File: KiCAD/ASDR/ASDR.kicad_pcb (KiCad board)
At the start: 2 copper layers, 50 x 100 mm, 43 parts, among them J1 IN, J2 OUT, J3 OUT, J4 Conn_01x03, J5 Conn_01x03, Q1 BC550, Q2 BC550, Q3 BC550, Q4 BC547, SW1 SW_SPDT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

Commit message: Review
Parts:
- R7, R8: value 100 -> 100R
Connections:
- J1 pad G: Net-(J1-PadG) -> GND
- J1 pad S: Net-(J1-PadG) -> GND
- RV2 pad 1: Net-(D2-K) -> Net-(R10-Pad1)
- RV2 pad 3: Net-(R10-Pad1) -> Net-(D2-K)
- RV3 pad 1: Net-(R7-Pad1) -> Net-(D3-A)
- RV3 pad 3: Net-(D3-A) -> Net-(R7-Pad1)
- RV4 pad 1: Net-(R8-Pad1) -> Net-(D4-K)
- RV4 pad 3: Net-(D4-K) -> Net-(R8-Pad1)
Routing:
- net Net-(Q1-C): track 3.88 -> 18.0 mm
- net Net-(U3B--): track 2.54 -> 10.8 mm
- net Net-(D4-K): track 13.8 -> 7.82 mm
- net Net-(D3-A): track 7.82 -> 12.8 mm
- net Net-(R10-Pad1): track 8.52 -> 12.8 mm
- net Net-(D2-K): track 21.4 -> 23.9 mm
- net Net-(R7-Pad1): track 16.8 -> 14.3 mm
- net Net-(R8-Pad1): track 15.3 -> 16.8 mm
- net Net-(Q2-C): track 51.4 -> 50.4 mm

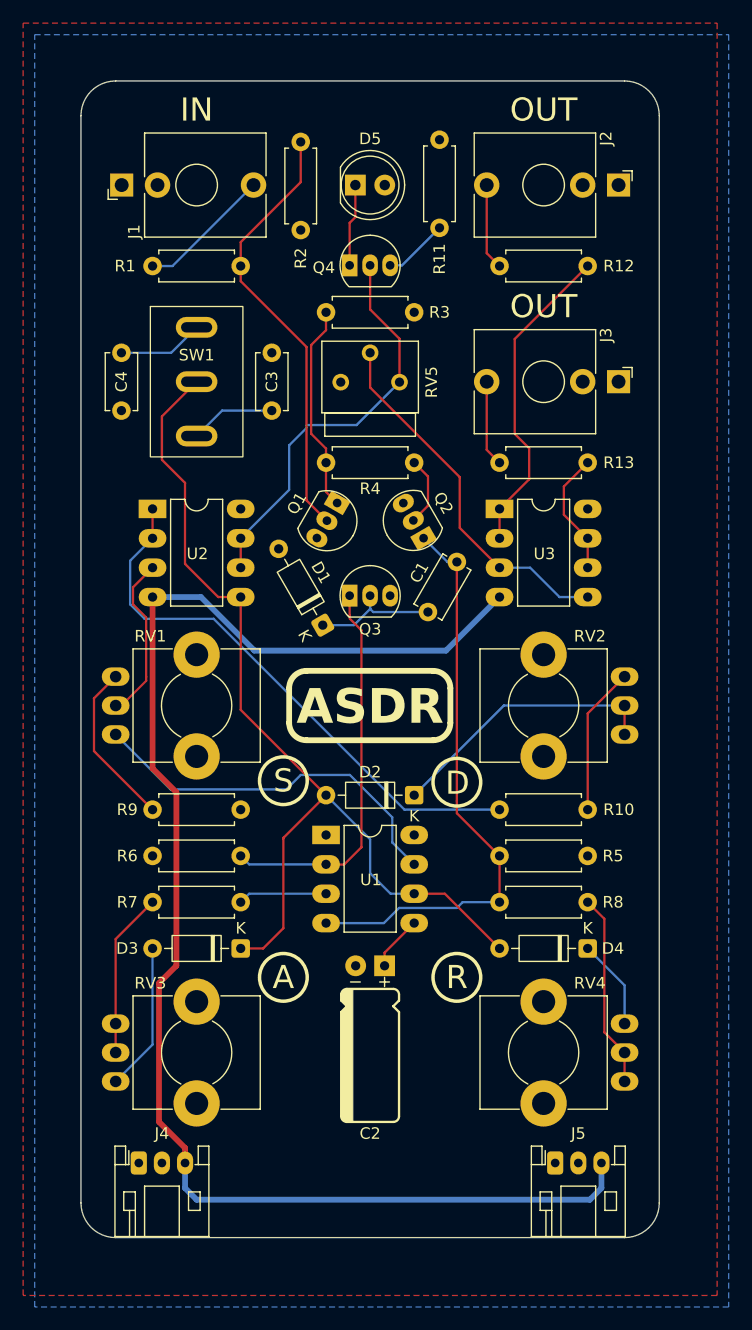
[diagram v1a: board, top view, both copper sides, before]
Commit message: ADSR Rearrange
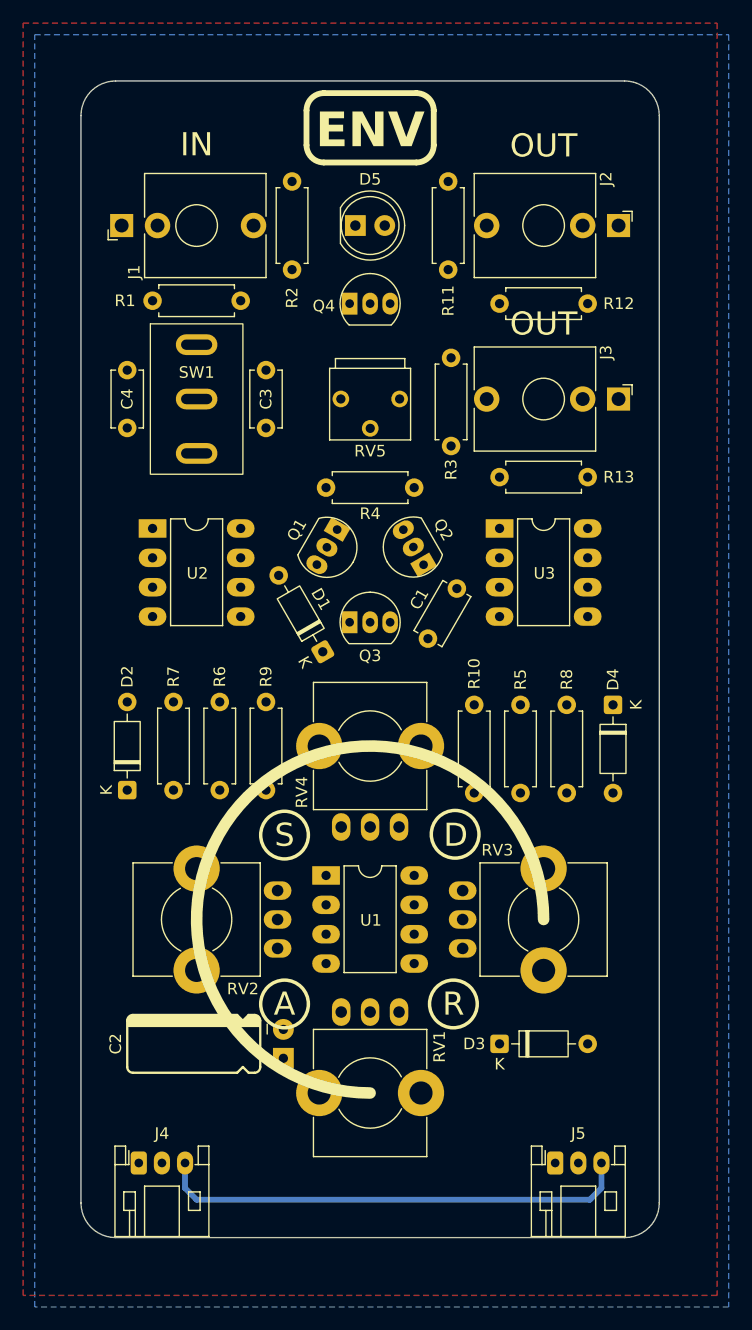
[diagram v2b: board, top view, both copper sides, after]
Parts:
- moved Ref** 48.1 mm to (136.0, 57.0)
- moved Ref** 48.0 mm to (164.2, 56.8)
- moved RV1 36.7 mm to (150.0, 137.5), turned to 180 degrees
- moved RV2 35.2 mm to (135.0, 122.5)
- moved RV3 32.1 mm to (165.0, 122.5)
- moved RV4 30.5 mm to (150.0, 107.5), turned to 0 degrees
- moved D2 24.8 mm to (129.0, 111.3), turned to 90 degrees
- moved D3 23.9 mm to (161.2, 133.2), turned to 0 degrees
- moved D4 21.2 mm to (171.0, 103.9), turned to -90 degrees
- moved R7 17.4 mm to (133.0, 103.7), turned to -90 degrees
- moved R8 17.2 mm to (167.0, 103.9), turned to -90 degrees
- moved R3 15.8 mm to (157.0, 81.6), turned to 90 degrees
- moved R6 13.4 mm to (137.0, 103.7), turned to -90 degrees
- moved R10 13.4 mm to (159.0, 103.9), turned to -90 degrees
- moved C2 10.1 mm to (142.5, 133.3), turned to 90 degrees
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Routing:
- net VSS: track 126.4 -> 41.2 mm
- net Net-(D2-A): track 83.7 -> 0.00 mm
- net Net-(Q2-C): track 50.4 -> 0.00 mm
- net Net-(U2A--): track 48.3 -> 0.00 mm
- net Net-(Q1-B): track 38.0 -> 0.00 mm
- net Net-(Q4-B): track 35.4 -> 0.00 mm
- net Net-(Q3-C): track 33.5 -> 0.00 mm
- net Net-(U1-DIS): track 32.8 -> 0.00 mm
- net Net-(U3A-+): track 31.9 -> 0.00 mm
- net Net-(U3A--): track 27.7 -> 0.00 mm
- net Net-(D2-K): track 23.9 -> 0.00 mm
- net Net-(Q1-C): track 18.0 -> 0.00 mm
- net Net-(R8-Pad1): track 16.8 -> 0.00 mm
- net Net-(R9-Pad2): track 15.4 -> 0.00 mm
- net Net-(U2A-+): track 14.5 -> 0.00 mm
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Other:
- board text added: "ENV"
- board text removed: "ASDR"

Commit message: VCF PCB
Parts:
- moved R13 0.95 mm to (161.2, 85.2)
- moved R3 0.38 mm to (156.7, 81.4)
- moved R11 0.15 mm to (156.6, 58.7)
- moved R2 0.15 mm to (143.4, 66.3)
- turned RV5 to 0 degrees
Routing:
- net Net-(D2-A): track 0.00 -> 110.3 mm, vias 0 -> 1
- net VSS: track 41.2 -> 122.2 mm
- net Net-(Q2-C): track 0.00 -> 52.0 mm, vias 0 -> 1
- net Net-(U2A-+): track 0.00 -> 49.8 mm
- net Net-(U2A--): track 0.00 -> 42.1 mm, vias 0 -> 1
- net Net-(R7-Pad1): track 0.00 -> 38.8 mm, vias 0 -> 1
- net Net-(Q3-C): track 0.00 -> 37.8 mm
- net Net-(Q1-B): track 0.00 -> 36.6 mm
- net Net-(Q4-B): track 0.00 -> 33.0 mm
- net Net-(U3A-+): track 0.00 -> 32.1 mm
- net Net-(R9-Pad2): track 0.00 -> 31.6 mm
- net Net-(R10-Pad1): track 0.00 -> 27.5 mm, vias 0 -> 1
- net Net-(U3A--): track 0.00 -> 25.2 mm
- net Net-(R8-Pad1): track 0.00 -> 24.6 mm
- net Net-(D2-K): track 0.00 -> 23.9 mm
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
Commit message: VCF PCB
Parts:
- C2: footprint HackSynth:CP_Radial_D5.2mm_P2.50mm_LayDown -> HackSynth:CP_Radial_D4.0mm_P1.50mm
- moved C2 22.9 mm to (165.0, 137.5), turned to 0 degrees
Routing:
- net Net-(U1-CV): track 17.1 -> 34.9 mm

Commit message: Footprint Edits
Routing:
- net Net-(U1-CV): track 34.9 -> 17.8 mm
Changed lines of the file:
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@@
 		)
 		(group ""
-			(members "01d04b5b-5a68-4add-86a7-c921b8d4927d" "22b10ea6-8a0e-44cb-8adf-3310c9d8c3c4"
-				"24896000-3ef7-42be-8b25-e165ea7e2f3f" "2ba23b84-2a03-461c-81bb-ab0d3cef5f97"
-				"4158b41c-4c4e-407b-a6f4-d5adbafdad55" "4159ada9-a120-4adc-88a5-a5a38e974d1f"
-				"4a0b4556-8de8-4ee1-b7eb-ff2eedacb006" "501e0701-3ab3-417e-be57-adb8f499f128"
-				"552f7810-4679-49b5-a2d4-570a0fb1fb11" "58be7fcb-ea43-4042-bac5-de700d4991c3"
-				"5c971b8b-ffea-45ff-a72f-af66a05ca55b" "62511e51-950f-48be-89bf-4ad477d81cd2"
-				"6456e14c-a747-437e-a713-751bef032803" "6a760896-c934-459c-8b68-4f1d0e8fe8be"
-				"6f0c5c0b-2703-4396-af2f-e140b0df8898" "78337fa1-a58c-4865-bf18-c5336d43f401"
-				"7c30f9fa-5e2b-4220-a57c-2f4d86562d5f" "7cbf7f97-5e14-4128-90b2-9f2698ec7ffa"
-				"820d5ae0-44ef-45bc-b8fa-ca06f942b5b6" "88fa4fee-ba6b-46a1-bcc1-cdea34fbf65a"
-				"89810525-cc48-4c70-8b78-ae36e64ede5e" "8bde54ec-a3a9-49d5-820b-99765d888603"
-				"8c93a84c-5a4d-444e-a861-7c8b6e76ba9f" "8ff09b30-ed0e-48ce-a25c-bea687aac8c9"
-				"93befb58-b544-456a-bde6-b5f15b4258a2" "9be824af-ac27-4f9e-bbf8-e566308d1356"
-				"9c594654-d431-46c4-b22f-439e5586859b" "a0eef203-311f-499f-9ace-8092bdad27fb"
-				"a2096fee-1087-4f78-9c22-45233cdc80e2" "a8339eed-bf9b-40da-9928-632c7f74b8d7"
-				"ab667063-22cd-44e6-a06d-395ef31fcba7" "b167a3ff-9a1f-4386-9356-d3d61a8d42ed"
-				"bb059476-5a20-4c6b-b62c-8b9f34f41326" "cc454877-d36c-4f08-8348-ba21a595b2c8"
-				"d05479ed-8f9e-4a3e-ab68-3df5c7532662" "d204c2e4-5605-4031-aa44-7010ce2a0417"
-				"d2e19fde-4eb9-4de3-9a36-4811358702bc" "d6214a36-0cb3-4fa0-ab97-f719c87ec91f"
-				"e30e94a7-594f-4656-9131-eaa07b449fb1" "e340d107-2614-4569-b29b-1ca70cef7df7"
-				"e7988d57-fc4f-4cf7-8403-1a9b863b7b61" "eceaee16-382a-4314-a712-94d7184ddd86"
-				"ef3c6bbe-9009-496f-a48d-6834fc32d452" "f91123de-83d1-416f-9923-04dc44631a43"
+			(members "00fef2d3-647e-45e4-9f71-eb2d56797821" "0ba1d85a-2985-41ac-8df2-3e260cde00c4"
+				"11ea94d3-bd34-4004-8ffe-271e3897d1e8" "199239b7-9bf3-43b6-a2bb-d594cd84d885"
+				"1d60629d-e647-42bb-bba5-dec1d1149755" "22138f32-b66d-4087-998c-e4b25464f814"
+				"2fb21eb0-f677-4ccc-89c1-db34939583a4" "389b1c07-eeab-43ac-95d4-f18c1128c5a9"
+				"3aa13e88-0175-4245-8008-6cc554015f14" "3d2724c9-20de-43ff-89fc-74ace2b7f2b3"
+				"47220ff9-2f75-4e15-9fc2-e36d656be937" "5416bb18-745e-4185-9362-103100331d2e"
+				"5b431fbb-cb1f-4d9b-811d-e303c3a85cb5" "5c654ba2-2a71-46e8-8595-989fa13180c3"
+				"6781b47e-2d6c-4c10-963b-3a67e06166b2" "67f575bc-18c2-4431-8d37-8cd933dbedfc"
+				"74ff93d1-b580-40d0-a57d-09419ade79db" "777350ff-f77c-49f9-aaa8-e2a040e7eae5"
+				"7872489f-6cf4-491b-8bd8-320c0f8be8a4" "792ef7d4-6ea1-4bed-969e-9ef0fb92a134"
+				"7c23f848-788f-4a73-a0fa-58039d798626" "82a7b0bd-0265-45d8-a7dd-a2f9316644fb"
+				"942a6a14-10ec-45b1-af9a-809662edf1fe" "9445e179-9422-459e-92a1-20d54b0706d1"
+				"976623b0-355e-4410-bc88-52c6c96f012f" "a0cb1465-a16a-43f3-b430-7dae3c54ced3"
+				"a442fe10-b74a-4d13-9132-bd6da348c0a3" "afbd7819-e28a-4236-bcd5-7b64ad2048af"
+				"b04403cf-86b5-46ce-aa10-bc23e14ccfe9" "b277062e-c614-4d43-8ac3-85d51bd152ef"
+				"b5cfa53a-8594-4f9a-924d-f1321018ec23" "b6f920d2-35f9-4d99-baa3-6139d8a455f8"
+				"c1a5a4aa-5193-42bc-a09f-10fbf9883996" "c29122bf-5182-4611-8537-898b32c841da"
+				"c6fdd8b0-9954-40e6-9799-be579ede83cb" "cd77e88c-9870-4d6b-b638-ce3820e6e82a"
+				"d0b8f695-4fdb-4ff1-b69b-f5967637b750" "d1f7ca02-802a-41df-af76-ee5b2da4d7a2"
+				"d8777f1d-0580-4396-a742-14f79d0106ab" "df33d521-95a7-4507-b11e-e22055d8633e"
+				"e9c9eb65-3aae-40a4-b374-e712cc375125" "eed1418a-2b16-41c3-8ed4-c1aa641edcde"
+				"ef038a7f-97fd-4801-aa62-645ecea5f3d8" "f6377cc7-aa3e-4e0a-9b26-179c2561ed57"
 			)
 		)
@@
 		(tags "CP Radial series Radial pin pitch 1.50mm diameter 4mm height 7mm Electrolytic Capacitor")
 		(property "Reference" "C2"
-			(at 0 -3.25 0)
+			(at -3.5 0 0)
 			(layer "F.SilkS")
 			(effects
@@
 		)
 		(fp_line
-			(start 1.6 -1.351)
-			(end 1.6 1.351)
-			(stroke
-				(width 0.12)
-				(type solid)
-			)
-			(layer "F.SilkS")
-		)
-		(fp_line
 			(start 1.64 -1.303)
 			(end 1.64 1.303)
@@
 		)
 		(pad "1" thru_hole roundrect
-			(at -0.75 0)
-			(size 1.2 1.2)
+			(at -0.9 0)
+			(size 1.3 1.3)
 			(drill 0.6)
 			(layers "*.Cu" "*.Mask")
@@
 		)
 		(pad "2" thru_hole circle
-			(at 0.75 0)
-			(size 1.2 1.2)
+			(at 0.9 0)
+			(size 1.3 1.3)
 			(drill 0.6)
 			(layers "*.Cu" "*.Mask")
@@
 		(net 4)
 	)
-	(segment
-		(start 148.75 131.505049)
-		(end 148.75 127.4171)
-		(width 0.2)
-		(layer "B.Cu")
-		(net 4)
-	)
-	(segment
-		(start 142.5 134.500001)
-		(end 145.755048 134.500001)
-		(width 0.2)
-		(layer "B.Cu")
-		(net 4)
-	)
-	(segment
-		(start 145.755048 134.500001)
-		(end 148.75 131.505049)
-		(width 0.2)
-		(layer "B.Cu")
-		(net 4)
-	)
-	(segment
-		(start 148.75 127.4171)
-		(end 149.8571 126.31)
-		(width 0.2)
-		(layer "B.Cu")
-		(net 4)
-	)
-	(segment
-		(start 149.8571 126.31)
-		(end 153.81 126.31)
-		(width 0.2)
-		(layer "B.Cu")
-		(net 4)
-	)
